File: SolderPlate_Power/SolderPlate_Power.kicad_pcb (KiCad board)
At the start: 2 copper layers, 104.5 x 22 mm, 22 parts, among them J1 N, J2 Fan, J3 L, J4 SSR, J5 LCD, J7 uCont, Q1 BSS138, Q2 BSS138, Q3 BSS138

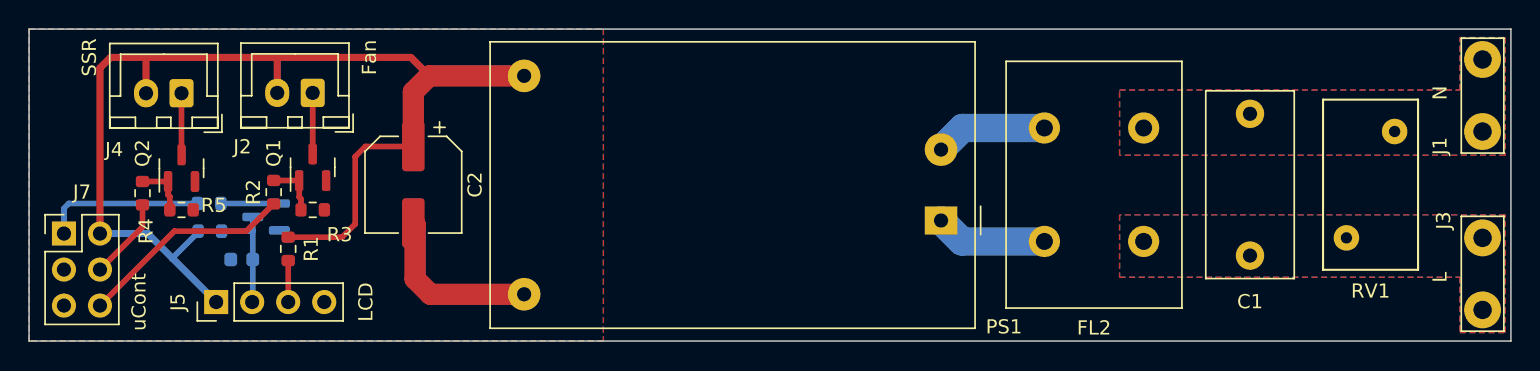
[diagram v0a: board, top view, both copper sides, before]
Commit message: Rounded power board edges
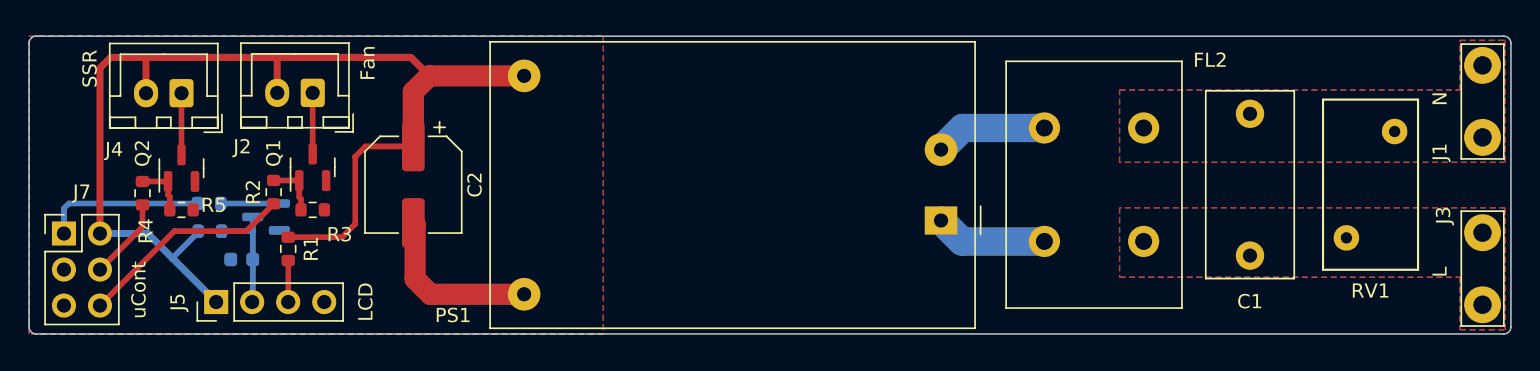
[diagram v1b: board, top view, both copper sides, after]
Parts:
- moved J1 0.41 mm to (189.0, 54.1)
- moved J3 0.37 mm to (189.0, 70.9)
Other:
- board size 104.5 x 22 mm -> 104.5 x 21 mm
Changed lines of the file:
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@@
   )
   (paper "A4")
+  (title_block
+    (title "SolderPlate Power Board")
+    (date "2023-04-21")
+    (rev "1.0")
+    (comment 1 "TiZed")
+  )
   (layers
     (0 "F.Cu" signal)
@@
     )
     (pad_to_mask_clearance 0)
+    (aux_axis_origin 86.5 73)
     (pcbplotparams
       (layerselection 0x00010fc_ffffffff)
@@
   (net 17 "unconnected-(J7-Pin_3-Pad3)")
   (footprint "TestPoint:TestPoint_Bridge_Pitch5.08mm_Drill1.3mm" (layer "F.Cu")
-    (at 189 71.305 90)
+    (at 189 70.94 90)
     (descr "wire loop as test point, pitch 5.08mm, hole diameter 1.3mm, wire diameter 1.0mm")
     (tags "test point wire loop")
@@
         (effects (font (size 1 1) (thickness 0.15)))
     )
-    (fp_text value "SSR" (at 6.5 2.525 90) (layer "F.SilkS")
+    (fp_text value "SSR" (at 6.45 1.725 90) (layer "F.SilkS")
         (effects (font (size 1 1) (thickness 0.15)))
     )
@@
     (property "ki_keywords" "EMI common mode filter")
     (attr through_hole)
-    (fp_text reference "FL2" (at 3.5 -6.1) (layer "F.SilkS")
+    (fp_text reference "FL2" (at -4.7 12.775) (layer "F.SilkS")
         (effects (font (size 1 1) (thickness 0.15)))
     )
@@
         (effects (font (size 1 1) (thickness 0.15)))
     )
-    (fp_text value "Fan" (at -4 2.5 90) (layer "F.SilkS")
+    (fp_text value "Fan" (at -3.9 2.1 90) (layer "F.SilkS")
         (effects (font (size 1 1) (thickness 0.15)))
     )
@@
         (effects (font (size 1 1) (thickness 0.15)))
     )
-    (fp_text value "uCont" (at 5.29 4.83 90) (layer "F.SilkS")
+    (fp_text value "uCont" (at 5.29 3.98 90) (layer "F.SilkS")
         (effects (font (size 1 1) (thickness 0.15)))
     )
@@
   )
   (footprint "TestPoint:TestPoint_Bridge_Pitch5.08mm_Drill1.3mm" (layer "F.Cu")
-    (at 189 53.645 -90)
+    (at 189 54.06 -90)
     (descr "wire loop as test point, pitch 5.08mm, hole diameter 1.3mm, wire diameter 1.0mm")
     (tags "test point wire loop")
@@
     (property "ki_keywords" "AC/DC module power supply")
     (attr through_hole)
-    (fp_text reference "PS1" (at -4.4375 -7.5 180) (layer "F.SilkS")
+    (fp_text reference "PS1" (at 34.4125 -6.7 180) (layer "F.SilkS")
         (effects (font (size 1 1) (thickness 0.15)))
     )
@@
     )
   )
-  (gr_rect (start 86.5 51.5) (end 191 73.5)
-    (stroke (width 0.1) (type default)) (fill none) (layer "Edge.Cuts"))
+  (gr_arc (start 191 72.5) (mid 190.853553 72.853553) (end 190.5 73)
+    (stroke (width 0.1) (type default)) (layer "Edge.Cuts"))
+  (gr_arc (start 87 73) (mid 86.646447 72.853553) (end 86.5 72.5)
+    (stroke (width 0.1) (type default)) (layer "Edge.Cuts"))
+  (gr_arc (start 190.5 52) (mid 190.853553 52.146447) (end 191 52.5)
+    (stroke (width 0.1) (type default)) (layer "Edge.Cuts"))
+  (gr_line (start 86.5 72.5) (end 86.5 52.5)
+    (stroke (width 0.1) (type default)) (layer "Edge.Cuts"))
+  (gr_arc (start 86.5 52.5) (mid 86.646447 52.146447) (end 87 52)
+    (stroke (width 0.1) (type default)) (layer "Edge.Cuts"))
+  (gr_line (start 190.5 73) (end 87 73)
+    (stroke (width 0.1) (type default)) (layer "Edge.Cuts"))
+  (gr_line (start 191 72.5) (end 191 52.5)
+    (stroke (width 0.1) (type default)) (layer "Edge.Cuts"))
+  (gr_line (start 87 52) (end 190.5 52)
+    (stroke (width 0.1) (type default)) (layer "Edge.Cuts"))
   (dimension (type aligned) (layer "Cmts.User")
     (pts (xy 191 73.5) (xy 86.5 73.5))
@@
   )
   (dimension (type aligned) (layer "Cmts.User")
-    (pts (xy 191 51.5) (xy 191 73.5))
+    (pts (xy 190.5 52) (xy 190.5 73))
     (height -4.25)
-    (gr_text "22.0000 mm" (at 194.1 62.5 90) (layer "Cmts.User")
+    (gr_text "21.0000 mm" (at 193.6 62.5 90) (layer "Cmts.User")
       (effects (font (size 1 1) (thickness 0.15)))
     )
@@
     (polygon
       (pts
-        (xy 86.5 51.5)
-        (xy 127 51.5)
-        (xy 127 73.5)
-        (xy 86.5 73.5)
+        (xy 86.5 52)
+        (xy 127 52)
+        (xy 127 73)
+        (xy 86.5 73)
       )
     )
@@
     (polygon
       (pts
-        (xy 190.6 72.9)
-        (xy 190.6 64.6)
-        (xy 163.4 64.6)
+        (xy 190.6 72.7)
+        (xy 190.6 64.1)
+        (xy 163.4 64.1)
         (xy 163.4 69)
         (xy 187.4 69)
-        (xy 187.4 72.9)
+        (xy 187.4 72.7)
       )
     )
@@
     (polygon
       (pts
-        (xy 190.6 52.1)
-        (xy 190.6 60.4)
-        (xy 163.4 60.4)
+        (xy 190.6 52.3)
+        (xy 190.6 60.9)
+        (xy 163.4 60.9)
         (xy 163.4 55.8)
         (xy 187.4 55.8)
-        (xy 187.4 52.1)
+        (xy 187.4 52.3)
       )
     )

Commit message: Shortend power supply board
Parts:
- moved R4 2.18 mm to (94.5, 60.9)
- moved J7 2.07 mm to (91.0, 65.9)
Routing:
- net /Contrast: track 11.3 -> 9.13 mm
- net /Fan_On: track 15.2 -> 13.2 mm
- net Net-(Q2-G): track 3.85 -> 5.84 mm
- net /SSR: track 5.80 -> 7.70 mm
- net +5V: track 80.0 -> 78.8 mm
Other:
- board size 104.5 x 21 mm -> 102 x 21 mm
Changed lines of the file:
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@@
   )
   (footprint "Resistor_SMD:R_0603_1608Metric" (layer "F.Cu")
-    (at 94.5 63.075 90)
+    (at 94.5 60.9 90)
     (descr "Resistor SMD 0603 (1608 Metric), square (rectangular) end terminal, IPC_7351 nominal, (Body size source: IPC-SM-782 page 72, https://www.pcb-3d.com/wordpress/wp-content/uploads/ipc-sm-782a_amendment_1_and_2.pdf), generated with kicad-footprint-generator")
     (tags "resistor")
@@
     (property "ki_keywords" "R resistor")
     (attr smd)
-    (fp_text reference "R4" (at -2.675 0.25 90) (layer "F.SilkS")
+    (fp_text reference "R4" (at -0.6 -1.8 180) (layer "F.SilkS")
         (effects (font (size 1 1) (thickness 0.15)))
     )
@@
     (property "ki_keywords" "connector")
     (attr through_hole)
-    (fp_text reference "J4" (at 4.75 -3.975) (layer "F.SilkS")
+    (fp_text reference "J4" (at 6.55 -2.775) (layer "F.SilkS")
         (effects (font (size 1 1) (thickness 0.15)))
     )
@@
     (property "ki_keywords" "N-Channel MOSFET")
     (attr smd)
-    (fp_text reference "Q2" (at 1.0625 -2.75 90) (layer "F.SilkS")
+    (fp_text reference "Q2" (at -0.5875 2.65 90) (layer "F.SilkS")
         (effects (font (size 1 1) (thickness 0.15)))
     )
@@
   )
   (footprint "Connector_PinHeader_2.54mm:PinHeader_2x03_P2.54mm_Vertical" (layer "F.Cu")
-    (at 88.96 65.92)
+    (at 91.025 65.92)
     (descr "Through hole straight pin header, 2x03, 2.54mm pitch, double rows")
     (tags "Through hole pin header THT 2x03 2.54mm double row")
@@
     (property "ki_keywords" "connector")
     (attr through_hole)
-    (fp_text reference "J7" (at 1.27 -2.92) (layer "F.SilkS")
-        (effects (font (size 1 1) (thickness 0.15)))
-    )
-    (fp_text value "uCont" (at 5.29 3.98 90) (layer "F.SilkS")
+    (fp_text reference "J7" (at -0.625 -2.72) (layer "F.SilkS")
+        (effects (font (size 1 1) (thickness 0.15)))
+    )
+    (fp_text value "uCont" (at 5.275 1.98 90) (layer "F.SilkS")
         (effects (font (size 1 1) (thickness 0.15)))
     )
@@
     (property "ki_keywords" "connector")
     (attr through_hole)
-    (fp_text reference "J5" (at 0 -2.695 90) (layer "F.SilkS")
+    (fp_text reference "J5" (at -0.95 -2.695 90) (layer "F.SilkS")
         (effects (font (size 1 1) (thickness 0.15)))
     )
@@
   (gr_arc (start 191 72.5) (mid 190.853553 72.853553) (end 190.5 73)
     (stroke (width 0.1) (type default)) (layer "Edge.Cuts"))
-  (gr_arc (start 87 73) (mid 86.646447 72.853553) (end 86.5 72.5)
+  (gr_arc (start 89.5 73) (mid 89.146447 72.853553) (end 89 72.5)
     (stroke (width 0.1) (type default)) (layer "Edge.Cuts"))
   (gr_arc (start 190.5 52) (mid 190.853553 52.146447) (end 191 52.5)
     (stroke (width 0.1) (type default)) (layer "Edge.Cuts"))
-  (gr_line (start 86.5 72.5) (end 86.5 52.5)
+  (gr_line (start 89 72.5) (end 89 52.5)
     (stroke (width 0.1) (type default)) (layer "Edge.Cuts"))
-  (gr_arc (start 86.5 52.5) (mid 86.646447 52.146447) (end 87 52)
+  (gr_arc (start 89 52.5) (mid 89.146447 52.146447) (end 89.5 52)
     (stroke (width 0.1) (type default)) (layer "Edge.Cuts"))
-  (gr_line (start 190.5 73) (end 87 73)
+  (gr_line (start 190.5 73) (end 89.5 73)
     (stroke (width 0.1) (type default)) (layer "Edge.Cuts"))
   (gr_line (start 191 72.5) (end 191 52.5)
     (stroke (width 0.1) (type default)) (layer "Edge.Cuts"))
-  (gr_line (start 87 52) (end 190.5 52)
+  (gr_line (start 89.5 52) (end 190.5 52)
     (stroke (width 0.1) (type default)) (layer "Edge.Cuts"))
   (dimension (type aligned) (layer "Cmts.User")
-    (pts (xy 191 73.5) (xy 86.5 73.5))
+    (pts (xy 191 74) (xy 89 74))
     (height -3.25)
-    (gr_text "104.5000 mm" (at 138.75 75.6) (layer "Cmts.User")
+    (gr_text "102.0000 mm" (at 140 76.1) (layer "Cmts.User")
       (effects (font (size 1 1) (thickness 0.15)))
     )
@@
   (segment (start 109.5 60.5) (end 110.225 59.775) (width 0.4) (layer "F.Cu") (net 2))
   (segment (start 104 53.5) (end 94.75 53.5) (width 0.5) (layer "F.Cu") (net 2))
-  (segment (start 92.25 53.5) (end 94.75 53.5) (width 0.5) (layer "F.Cu") (net 2))
+  (segment (start 93.565 63.965) (end 93.565 65.92) (width 0.5) (layer "F.Cu") (net 2))
   (segment (start 104.775 66.175) (end 108.575 66.175) (width 0.4) (layer "F.Cu") (net 2))
   (segment (start 109.5 65.25) (end 109.5 60.5) (width 0.4) (layer "F.Cu") (net 2))
   (segment (start 121.4125 54.8) (end 114.725 54.8) (width 1.5) (layer "F.Cu") (net 2))
+  (segment (start 94.75 53.5) (end 92.25 53.5) (width 0.5) (layer "F.Cu") (net 2))
   (segment (start 113.6 55.925) (end 113.6 59.775) (width 1.5) (layer "F.Cu") (net 2))
   (segment (start 104 56) (end 104 53.5) (width 0.5) (layer "F.Cu") (net 2))
   (segment (start 108.575 66.175) (end 109.5 65.25) (width 0.4) (layer "F.Cu") (net 2))
+  (segment (start 92.25 53.5) (end 91.5 54.25) (width 0.5) (layer "F.Cu") (net 2))
   (segment (start 113.425 53.5) (end 114.725 54.8) (width 0.5) (layer "F.Cu") (net 2))
   (segment (start 94.75 53.5) (end 94.75 56.025) (width 0.5) (layer "F.Cu") (net 2))
-  (segment (start 91.5 54.25) (end 92.25 53.5) (width 0.5) (layer "F.Cu") (net 2))
-  (segment (start 91.5 65.92) (end 91.5 54.25) (width 0.5) (layer "F.Cu") (net 2))
+  (segment (start 91.5 54.25) (end 91.5 61.9) (width 0.5) (layer "F.Cu") (net 2))
+  (segment (start 91.5 61.9) (end 93.565 63.965) (width 0.5) (layer "F.Cu") (net 2))
   (segment (start 104 53.5) (end 113.425 53.5) (width 0.5) (layer "F.Cu") (net 2))
   (segment (start 110.225 59.775) (end 113.6 59.775) (width 0.4) (layer "F.Cu") (net 2))
   (segment (start 114.725 54.8) (end 113.6 55.925) (width 1.5) (layer "F.Cu") (net 2))
   (segment (start 96.5975 67.6525) (end 99.695 70.75) (width 0.5) (layer "B.Cu") (net 2))
-  (segment (start 91.5 65.92) (end 94.865 65.92) (width 0.5) (layer "B.Cu") (net 2))
+  (segment (start 94.865 65.92) (end 93.565 65.92) (width 0.5) (layer "B.Cu") (net 2))
   (segment (start 98.425 65.825) (end 96.5975 67.6525) (width 0.4) (layer "B.Cu") (net 2))
   (segment (start 98.425 65.75) (end 98.425 65.825) (width 0.4) (layer "B.Cu") (net 2))
   (segment (start 94.865 65.92) (end 96.5975 67.6525) (width 0.5) (layer "B.Cu") (net 2))
-  (segment (start 113.725 65.3) (end 113.6 65.175) (width 1.5) (layer "F.Cu") (net 3))
-  (segment (start 114.8 70.2) (end 113.725 69.125) (width 1.5) (layer "F.Cu") (net 3))
+  (segment (start 113.6 69) (end 113.6 65.175) (width 1.5) (layer "F.Cu") (net 3))
   (segment (start 121.4125 70.2) (end 114.8 70.2) (width 1.5) (layer "F.Cu") (net 3))
-  (segment (start 113.725 69.125) (end 113.725 65.3) (width 1.5) (layer "F.Cu") (net 3))
+  (segment (start 114.8 70.2) (end 113.6 69) (width 1.5) (layer "F.Cu") (net 3))
   (segment (start 158.1 66.475) (end 152.2875 66.475) (width 2) (layer "B.Cu") (net 4))
   (segment (start 152.2875 66.475) (end 150.8125 65) (width 2) (layer "B.Cu") (net 4))
@@
   (segment (start 105.55 63.35) (end 105.55 62.1875) (width 0.4) (layer "F.Cu") (net 6))
   (segment (start 104.775 67.825) (end 104.775 70.75) (width 0.4) (layer "F.Cu") (net 7))
-  (segment (start 96.75 65.75) (end 101.825 65.75) (width 0.4) (layer "F.Cu") (net 8))
+  (segment (start 98.815 65.75) (end 93.565 71) (width 0.4) (layer "F.Cu") (net 8))
+  (segment (start 101.825 65.75) (end 98.815 65.75) (width 0.4) (layer "F.Cu") (net 8))
   (segment (start 101.825 65.75) (end 103.75 63.825) (width 0.4) (layer "F.Cu") (net 8))
-  (segment (start 91.5 71) (end 96.75 65.75) (width 0.4) (layer "F.Cu") (net 8))
   (segment (start 106.5 60.3125) (end 106.5 56) (width 0.4) (layer "F.Cu") (net 9))
   (segment (start 97.25 60.375) (end 97.25 56.025) (width 0.4) (layer "F.Cu") (net 11))
+  (segment (start 96.3 60.4) (end 96.3 62.25) (width 0.3) (layer "F.Cu") (net 12))
+  (segment (start 94.5 60.075) (end 95.975 60.075) (width 0.3) (layer "F.Cu") (net 12))
   (segment (start 96.3 63.2) (end 96.3 62.25) (width 0.4) (layer "F.Cu") (net 12))
-  (segment (start 96.3 62.25) (end 94.5 62.25) (width 0.4) (layer "F.Cu") (net 12))
+  (segment (start 95.975 60.075) (end 96.3 60.4) (width 0.3) (layer "F.Cu") (net 12))
   (segment (start 96.425 63.325) (end 96.3 63.2) (width 0.4) (layer "F.Cu") (net 12))
   (segment (start 96.425 64.25) (end 96.425 63.325) (width 0.4) (layer "F.Cu") (net 12))
-  (segment (start 91.5 68.46) (end 94.5 65.46) (width 0.4) (layer "F.Cu") (net 13))
-  (segment (start 94.5 65.46) (end 94.5 63.9) (width 0.4) (layer "F.Cu") (net 13))
+  (segment (start 95.2 66.825) (end 95.2 64.5) (width 0.3) (layer "F.Cu") (net 13))
+  (segment (start 95.2 64.5) (end 94.5 63.8) (width 0.3) (layer "F.Cu") (net 13))
+  (segment (start 93.565 68.46) (end 95.2 66.825) (width 0.3) (layer "F.Cu") (net 13))
+  (segment (start 94.5 63.8) (end 94.5 61.725) (width 0.3) (layer "F.Cu") (net 13))
   (segment (start 102.275 67.75) (end 102.275 70.71) (width 0.4) (layer "B.Cu") (net 14))
   (segment (start 102.275 65.75) (end 102.275 67.75) (width 0.4) (layer "B.Cu") (net 14))
@@
   (segment (start 102.275 70.71) (end 102.235 70.75) (width 0.4) (layer "B.Cu") (net 14))
   (segment (start 100.025 63.8) (end 104.15 63.8) (width 0.4) (layer "B.Cu") (net 15))
-  (segment (start 98.375 63.8) (end 89.3 63.8) (width 0.4) (layer "B.Cu") (net 16))
-  (segment (start 88.96 64.14) (end 88.96 65.92) (width 0.4) (layer "B.Cu") (net 16))
-  (segment (start 89.3 63.8) (end 88.96 64.14) (width 0.4) (layer "B.Cu") (net 16))
+  (segment (start 98.375 63.8) (end 91.6 63.8) (width 0.4) (layer "B.Cu") (net 16))
+  (segment (start 91.6 63.8) (end 91.025 64.375) (width 0.4) (layer "B.Cu") (net 16))
+  (segment (start 91.025 64.375) (end 91.025 65.92) (width 0.4) (layer "B.Cu") (net 16))
   (zone (net 3) (net_name "GND") (layers "F&B.Cu") (hatch edge 0.5)
     (connect_pads yes (clearance 0.2))
@@
     (polygon
       (pts
-        (xy 86.5 52)
+        (xy 89 52)
         (xy 127 52)
         (xy 127 73)
-        (xy 86.5 73)
+        (xy 89 73)
       )
     )
